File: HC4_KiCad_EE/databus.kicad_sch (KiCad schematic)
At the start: 11 parts, among them IC10 74HC4002, IC8 74HC257, IC9 74HC244, J3 Expantion_Connector

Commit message: 一部を整地
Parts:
- removed IC10: 74HC4002, Package_DIP:DIP-14_W7.62mm_Socket, symbol 74xx_2:74HC4002
- removed IC8: 74HC257, Package_DIP:DIP-16_W7.62mm_Socket, symbol 74xx_2:74HC257
- removed J3: Expantion_Connector, Connector_PinHeader_2.54mm:PinHeader_2x20_P2.54mm_Vertical, symbol Connector_Generic:Conn_02x20_Odd_Even
- removed LD4, LD5, LD6, LD7: LED, LED_THT:LED_Rectangular_W5.0mm_H2.0mm, symbol Device2:LED_
- removed RN2: 1k, Resistor_THT:R_Array_SIP5, symbol Device:R_Network04_Split
- added IC1, IC5: 74HC374, symbol 74xx_2:74HC374
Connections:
- net ALU0: now also IC9.17 (2A0)
- net ALU1: now also IC9.15 (2A1)
- net ALU2: now also IC9.13 (2A2)
- net ALU3: now also IC9.11 (2A3)
- net Databus0: now also IC9.3 (2Y0); no longer IC9.17 (2A0)
- net Databus1: now also IC9.5 (2Y1); no longer IC9.15 (2A1)
- net Databus2: now also IC9.7 (2Y2); no longer IC9.13 (2A2)
- net Databus3: now also IC9.9 (2Y3); no longer IC9.11 (2A3)
- net GND: no longer IC9.19 (2OE)
- net ~{ALU_OE}: now also IC9.19 (2OE)
- no-connect marks 22 -> 0
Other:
- note removed: "Instruction_Decoder"

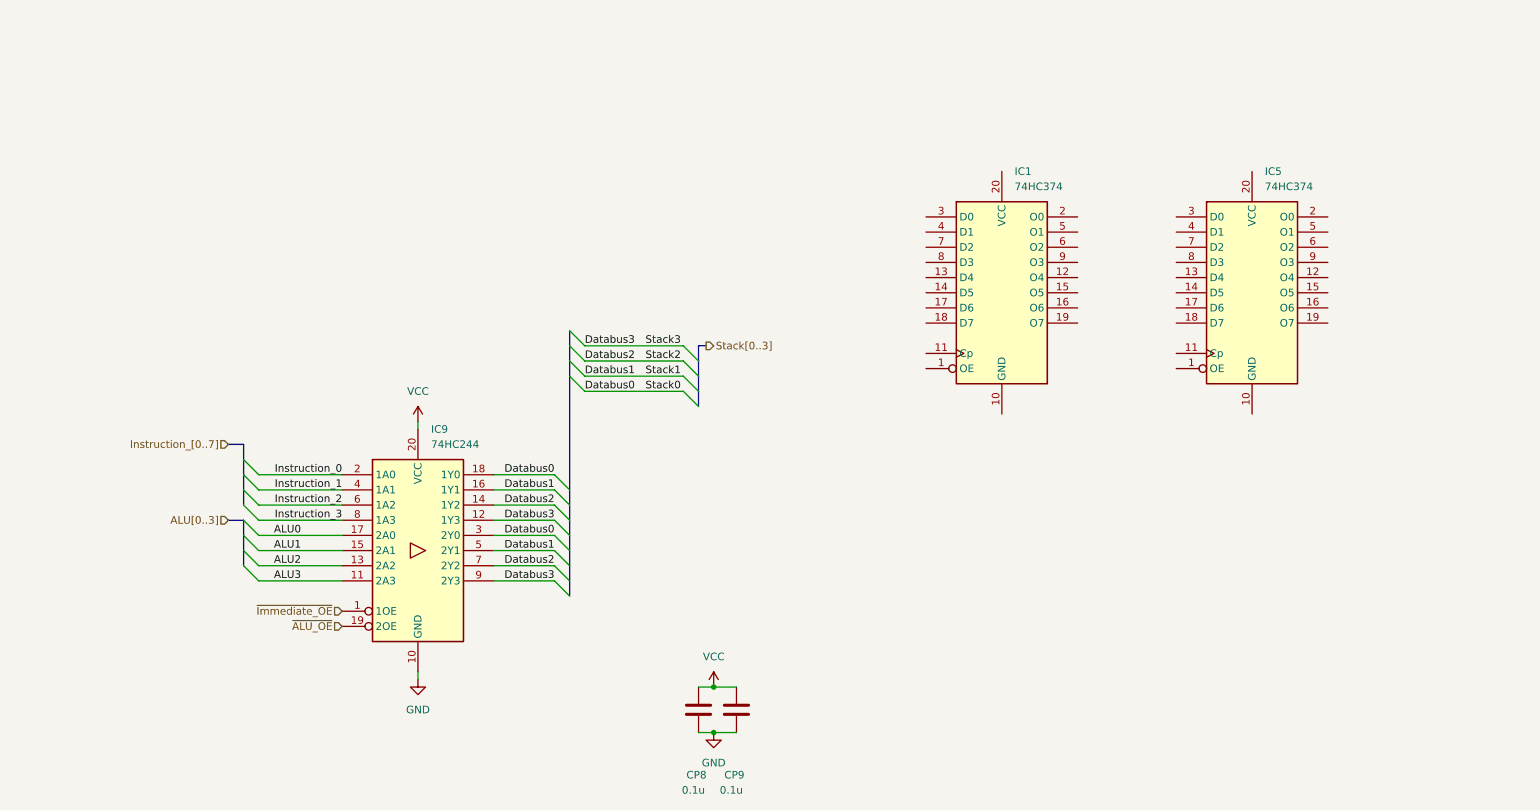
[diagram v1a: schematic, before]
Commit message: 4809を別シートに、ほか
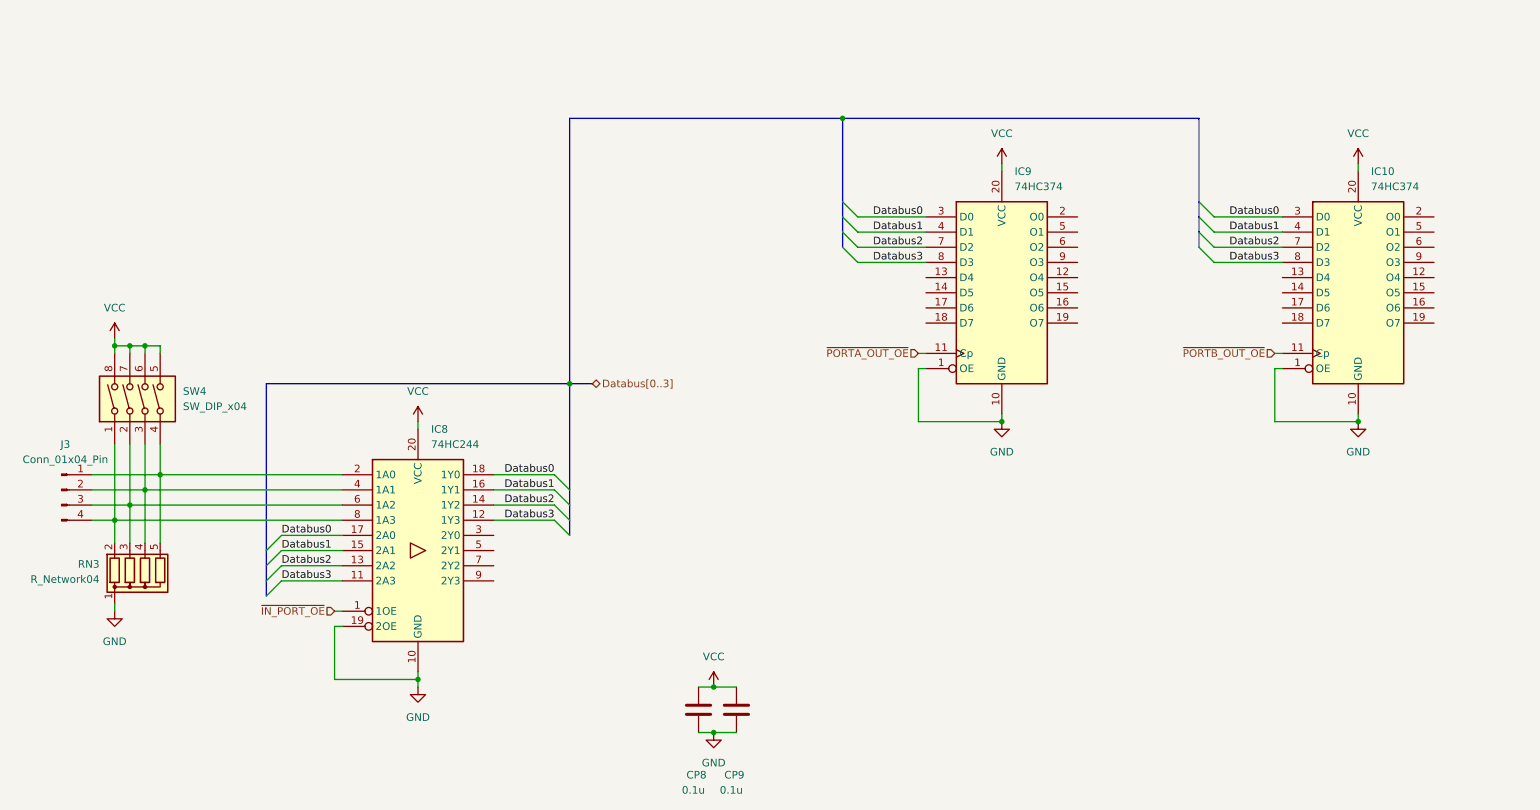
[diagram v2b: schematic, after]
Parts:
- added J3: Conn_01x04_Pin, symbol Connector:Conn_01x04_Pin
- added RN3: R_Network04, Resistor_THT:R_Array_SIP5, symbol Device:R_Network04
- added SW4: SW_DIP_x04, symbol Switch:SW_DIP_x04
- renumbered IC5 to IC10, IC9 to IC8, IC1 to IC9
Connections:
- net ALU0 is gone; now on net Databus0: IC8.17 (2A0)
- net ALU1 is gone; now on net Databus1: IC8.15 (2A1)
- net ALU2 is gone; now on net Databus2: IC8.13 (2A2)
- net ALU3 is gone; now on net Databus3: IC8.11 (2A3)
- net ~{ALU_OE} is gone; now on net GND: IC8.19 (2OE)
- net Databus0: now also IC10.3 (D0), IC9.3 (D0); no longer IC8.3 (2Y0)
- net Databus1: now also IC10.4 (D1), IC9.4 (D1); no longer IC8.5 (2Y1)
- net Databus2: now also IC10.7 (D2), IC9.7 (D2); no longer IC8.7 (2Y2)
- net Databus3: now also IC10.8 (D3), IC9.8 (D3); no longer IC8.9 (2Y3)
- net GND: now also IC10.1 (OE), IC10.10 (GND), IC9.1 (OE), IC9.10 (GND), RN3.1 (common)
- net VCC: now also IC10.20 (VCC), IC9.20 (VCC), SW4.5, SW4.6, SW4.7, SW4.8
- net ~{PORTA_OUT_OE}: now reaches IC9.11 (Cp)
- net ~{PORTB_OUT_OE}: now reaches IC10.11 (Cp)
- net Instruction_0: no longer names the net of IC8.2 (1A0)
- net Instruction_0: now also J3.1 (Pin_1), RN3.5 (R4), SW4.4
- net Instruction_1: no longer names the net of IC8.4 (1A1)
- net Instruction_1: now also J3.2 (Pin_2), RN3.4 (R3), SW4.3
- net Instruction_2: no longer names the net of IC8.6 (1A2)
- net Instruction_2: now also J3.3 (Pin_3), RN3.3 (R2), SW4.2
- net Instruction_3: no longer names the net of IC8.8 (1A3)
- net Instruction_3: now also J3.4 (Pin_4), RN3.2 (R1), SW4.1
- net ~{Immediate_OE} renamed ~{IN_PORT_OE}
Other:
- moved on the sheet: IC10

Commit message: 完成かも～
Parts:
- removed IC10, IC9: 74HC374, symbol 74xx_2:74HC374
- added CP11: 0.1u, Capacitor_THT:C_Disc_D3.0mm_W1.6mm_P2.50mm, symbol Device2:C_Bypass
- added IC6, IC7: 74HC377, symbol 74xx_2:74HC377
- added J3: Port_A, symbol Connector:Conn_01x04_Pin
- added J4: Port_B, symbol Connector:Conn_01x04_Pin
- added LD10, LD11, LD12, LD13, LD14, LD3, LD4, LD5, LD6, LD7, LD8, LD9: LED, LED_THT:LED_Rectangular_W5.0mm_H2.0mm, symbol Device2:LED_
- added RN2, RN3, RN4: 1k, Resistor_THT:R_Array_SIP9, symbol Device:R_Network08_Split
- J2: renamed from J3; value Conn_01x04_Pin -> Port_IN
- RN1: renamed from RN3; value R_Network04 -> 10k
- renumbered IC8 to IC5, SW4 to SW1
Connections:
- net Databus0: now also IC6.13 (D4), IC6.3 (D0), IC7.13 (D4), IC7.3 (D0)
- net Databus1: now also IC6.14 (D5), IC6.4 (D1), IC7.14 (D5), IC7.4 (D1)
- net Databus2: now also IC6.17 (D6), IC6.7 (D2), IC7.17 (D6), IC7.7 (D2)
- net Databus3: now also IC6.18 (D7), IC6.8 (D3), IC7.18 (D7), IC7.8 (D3)
- net GND: now also CP11.2, IC6.1 (~{E}), IC6.10 (GND), IC7.1 (~{E}), IC7.10 (GND), RN2.1 (R1), RN2.1 (R1), RN2.1 (R1), RN2.1 (R1), RN3.1 (R1), RN3.1 (R1), RN3.1 (R1), RN3.1 (R1), RN4.1 (R1), RN4.1 (R1), RN4.1 (R1), RN4.1 (R1)
- net VCC: now also CP11.1, IC6.20 (VCC), IC7.20 (VCC)
- net ~{PORTA_OUT_OE}: now also IC6.11 (CP)
- net ~{PORTB_OUT_OE}: now also IC7.11 (CP)
- net at IC5.3 (2Y0): now also LD6.2
- net at IC5.5 (2Y1): now also LD5.2
- net at IC5.7 (2Y2): now also LD4.2
- net at IC5.9 (2Y3): now also LD3.2
- new net: LD13.1 (K), RN4.4 (R3.2)
- new net: LD5.1 (K), RN2.4 (R3.2)
- new net: LD10.1 (K), RN3.5 (R4.2)
- new net: IC6.12 (Q4), LD10.2
- new net: LD14.1 (K), RN4.5 (R4.2)
- new net: IC7.12 (Q4), LD14.2
- new net: IC7.15 (Q5), LD13.2
- new net: LD12.1 (K), RN4.3 (R2.2)
- new net: LD6.1 (K), RN2.5 (R4.2)
- new net: IC6.15 (Q5), LD9.2
- new net: IC6.16 (Q6), LD8.2
- new net: IC6.19 (Q7), LD7.2
- new net: IC6.2 (Q0), J3.1 (Pin_1)
- new net: IC6.5 (Q1), J3.2 (Pin_2)
- new net: IC6.6 (Q2), J3.3 (Pin_3)
- new net: IC6.9 (Q3), J3.4 (Pin_4)
- new net: IC7.16 (Q6), LD12.2
- new net: IC7.2 (Q0), J4.1 (Pin_1)
- new net: IC7.5 (Q1), J4.2 (Pin_2)
- new net: IC7.6 (Q2), J4.3 (Pin_3)
- new net: IC7.9 (Q3), J4.4 (Pin_4)
- new net: LD8.1 (K), RN3.3 (R2.2)
- new net: LD11.1 (K), RN4.2 (R1.2)
- new net: LD9.1 (K), RN3.4 (R3.2)
- new net: IC7.19 (Q7), LD11.2
- new net: LD4.1 (K), RN2.3 (R2.2)
- new net: LD7.1 (K), RN3.2 (R1.2)
- new net: LD3.1 (K), RN2.2 (R1.2)

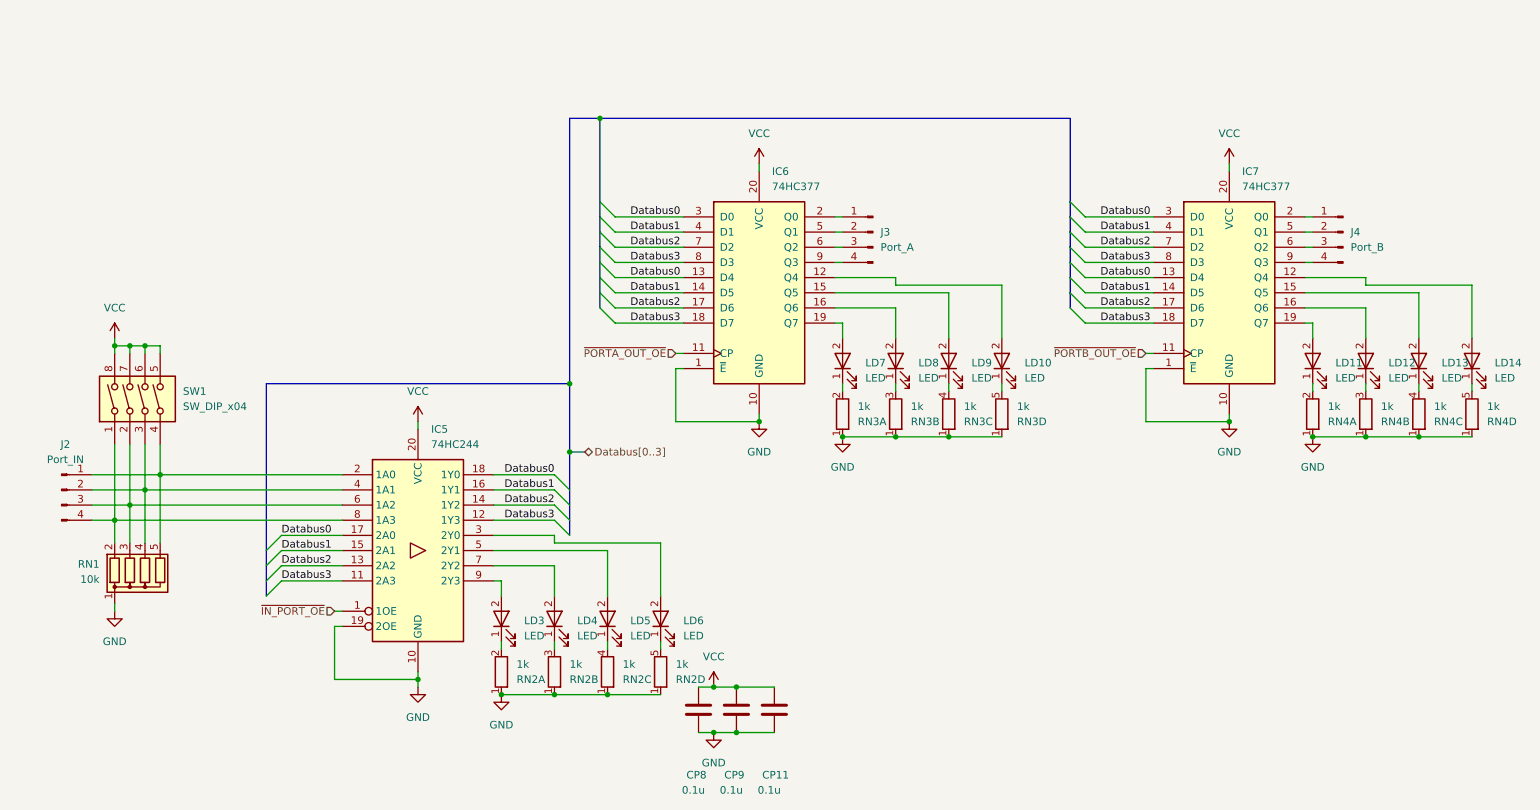
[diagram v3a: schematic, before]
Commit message: Carry_ENを論理反転、回路図の修正
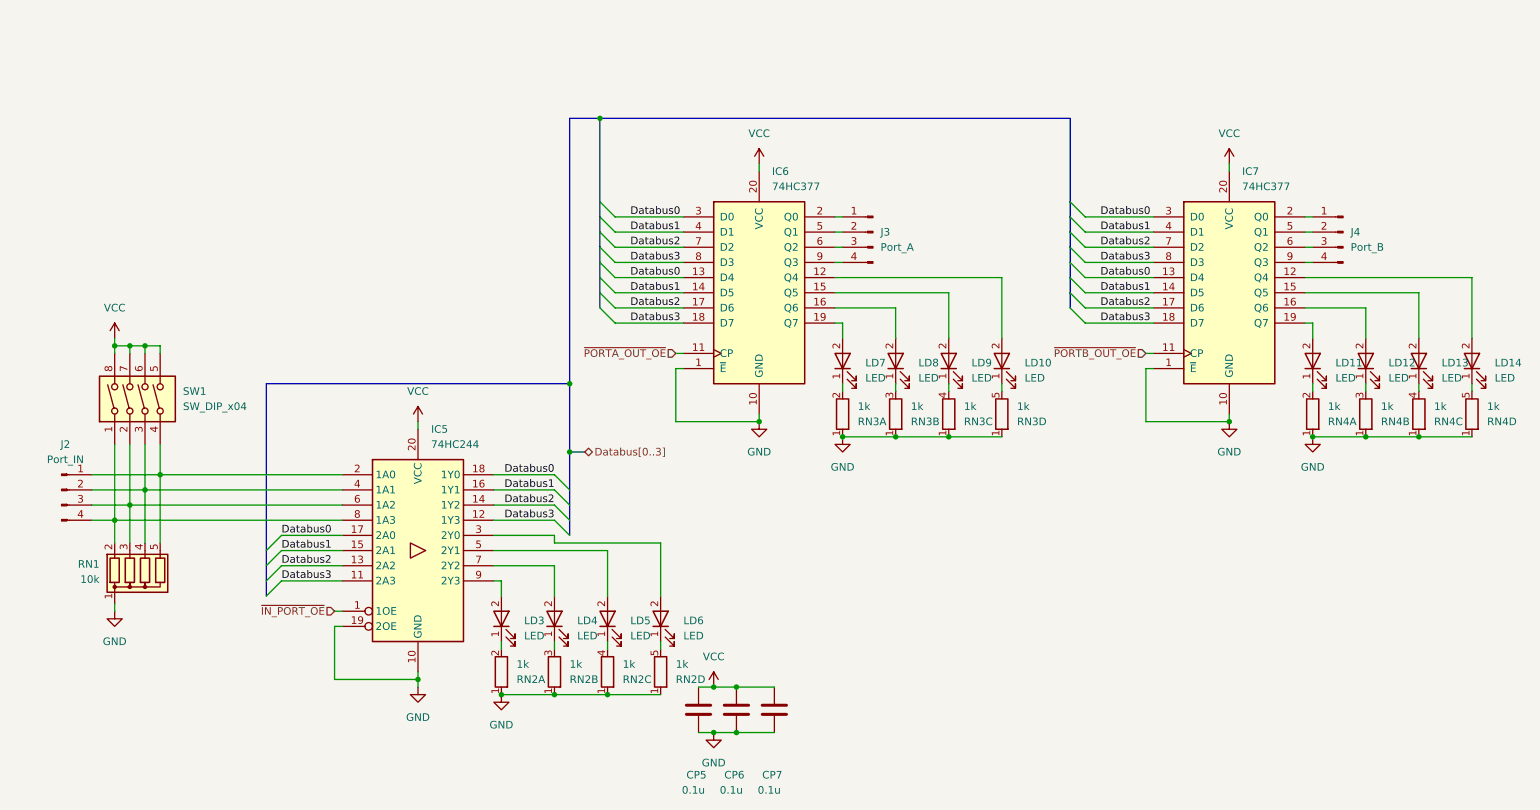
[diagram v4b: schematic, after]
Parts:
- renumbered CP8 to CP5, CP9 to CP6, CP11 to CP7
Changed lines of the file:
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@@
 	(wire
 		(pts
-			(xy 168.91 87.63) (xy 179.07 87.63)
+			(xy 168.91 87.63) (xy 196.85 87.63)
 		)
 		(stroke
@@
 	(wire
 		(pts
-			(xy 275.59 88.9) (xy 275.59 97.79)
+			(xy 275.59 87.63) (xy 275.59 97.79)
 		)
 		(stroke
@@
 	(wire
 		(pts
-			(xy 257.81 87.63) (xy 257.81 88.9)
-		)
-		(stroke
-			(width 0)
-			(type default)
-		)
-	)
-	(wire
-		(pts
 			(xy 132.08 95.25) (xy 143.51 95.25)
 		)
@@
 	(wire
 		(pts
-			(xy 257.81 88.9) (xy 275.59 88.9)
-		)
-		(stroke
-			(width 0)
-			(type default)
-		)
-	)
-	(wire
-		(pts
 			(xy 210.82 80.01) (xy 222.25 80.01)
 		)
@@
 	(wire
 		(pts
-			(xy 196.85 88.9) (xy 196.85 97.79)
+			(xy 196.85 87.63) (xy 196.85 97.79)
 		)
 		(stroke
@@
 		)
 	)
-	(wire
-		(pts
-			(xy 179.07 87.63) (xy 179.07 88.9)
-		)
-		(stroke
-			(width 0)
-			(type default)
-		)
-	)
-	(wire
-		(pts
-			(xy 179.07 88.9) (xy 196.85 88.9)
-		)
-		(stroke
-			(width 0)
-			(type default)
-		)
-	)
 	(bus
 		(pts
@@
 	(wire
 		(pts
-			(xy 247.65 87.63) (xy 257.81 87.63)
+			(xy 247.65 87.63) (xy 275.59 87.63)
 		)
 		(stroke
@@
 		(on_board yes)
 		(dnp no)
-		(property "Reference" "CP8"
+		(property "Reference" "CP5"
 			(at 144.018 170.942 0)
 			(effects
@@
 			(project "HC4_KiCad"
 				(path "/33731ded-38c0-4297-bdd8-92b082f46ff8/294cbb59-ed60-4be2-81ec-3da02c446083"
-					(reference "CP8")
+					(reference "CP5")
 					(unit 1)
 				)
@@
 		(on_board yes)
 		(dnp no)
-		(property "Reference" "CP11"
+		(property "Reference" "CP7"
 			(at 156.718 170.942 0)
 			(effects
@@
 			(project "HC4_KiCad_EE"
 				(path "/33731ded-38c0-4297-bdd8-92b082f46ff8/294cbb59-ed60-4be2-81ec-3da02c446083"
-					(reference "CP11")
+					(reference "CP7")
 					(unit 1)
 				)
@@
 		(on_board yes)
 		(dnp no)
-		(property "Reference" "CP9"
+		(property "Reference" "CP6"
 			(at 150.368 170.942 0)
 			(effects
@@
 			(project "HC4_KiCad"
 				(path "/33731ded-38c0-4297-bdd8-92b082f46ff8/294cbb59-ed60-4be2-81ec-3da02c446083"
-					(reference "CP9")
+					(reference "CP6")
 					(unit 1)
 				)

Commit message: PortBを4511に、フットプリントの割り付け開始
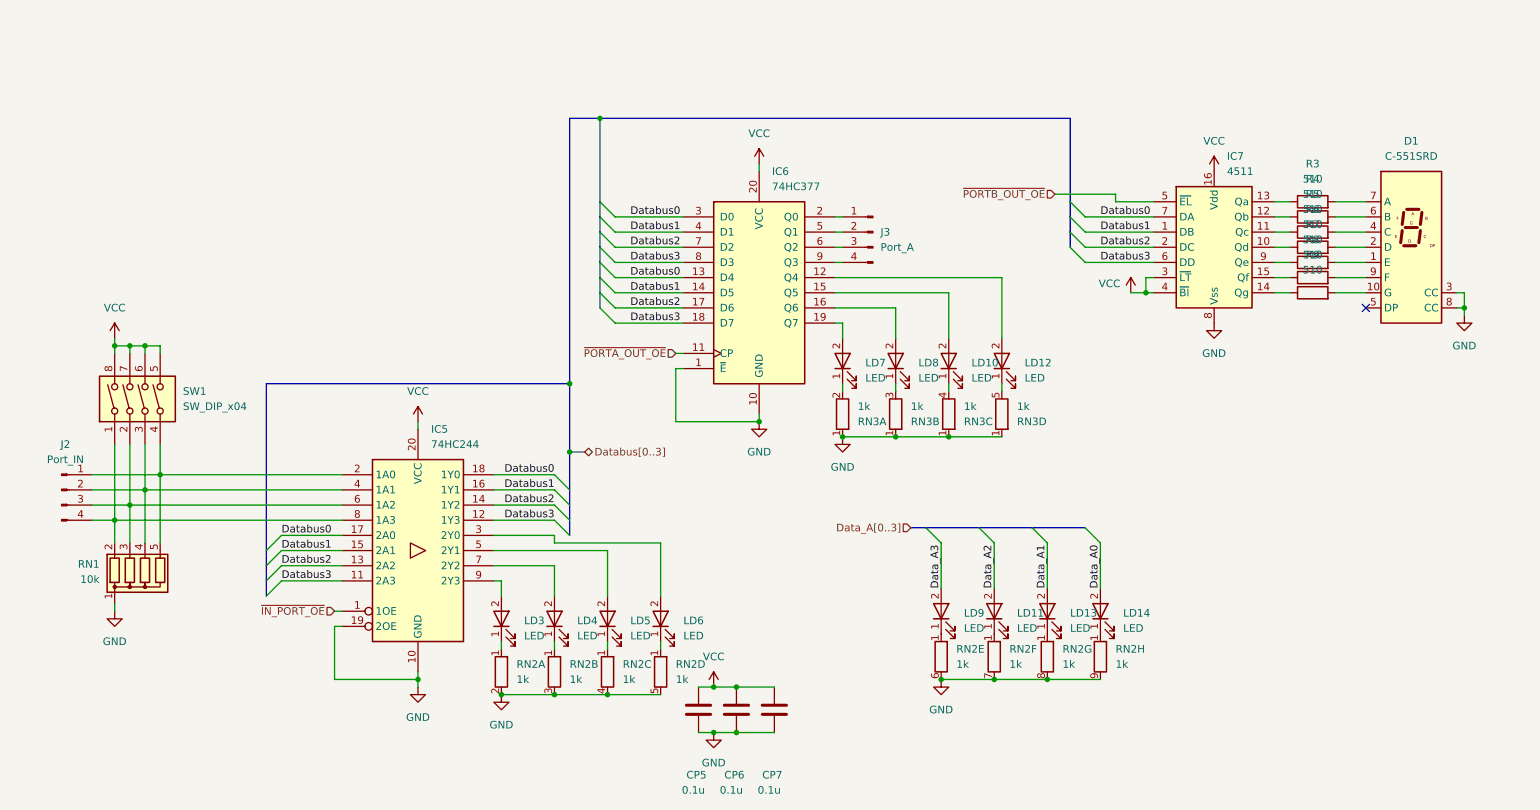
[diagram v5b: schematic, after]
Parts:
- removed IC7: 74HC377, symbol 74xx_2:74HC377
- removed J4: Port_B, symbol Connector:Conn_01x04_Pin
- removed LD12: LED, LED_THT:LED_Rectangular_W5.0mm_H2.0mm, symbol Device2:LED_
- removed RN4: 1k, Resistor_THT:R_Array_SIP9, symbol Device:R_Network08_Split
- added D1: C-551SRD, Display_7Segment:D1X8K, symbol Display_Character:D168K
- added IC7: 4511, symbol 4xxx_IEEE:4511
- added LD9: LED, LED_THT:LED_Rectangular_W5.0mm_H2.0mm, symbol Device2:LED_
- added R3, R4, R5, R6, R7, R8, R9: 510, symbol Device:R
- added unit 6 of RN2
- added unit 8 of RN2
- added unit 7 of RN2
- added unit 5 of RN2
- CP5, CP6, CP7: footprint Capacitor_THT:C_Disc_D3.0mm_W1.6mm_P2.50mm -> Capacitor_SMD:C_0603_1608Metric
- IC5: footprint Package_DIP:DIP-20_W7.62mm_Socket -> Package_SO:SOP-20_7.5x12.8mm_P1.27mm
- IC6: footprint (none) -> Package_SO:SOP-20_7.5x12.8mm_P1.27mm
- renumbered LD9 to LD10, LD10 to LD12
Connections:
- net Databus0: now also IC7.7 (DA)
- net Databus1: now also IC7.1 (DB)
- net Databus2: now also IC7.2 (DC)
- net Databus3: now also IC7.6 (DD)
- net GND: now also RN2.2 (R1.2), RN2.3 (R2.2), RN2.4 (R3.2), RN2.5 (R4.2), D1.3 (CC), D1.8 (CC), IC7.8 (Vss), RN2.6 (R5.2), RN2.7 (R6.2), RN2.8 (R7.2), RN2.9 (R8.2); no longer RN2.1 (R1), RN2.1 (R1), RN2.1 (R1), RN2.1 (R1)
- net VCC: now also IC7.16 (Vdd), IC7.3 (~{LT}), IC7.4 (~{BI})
- net ~{PORTB_OUT_OE}: now also IC7.5 (~{EL})
- net at LD13.1 (K): now also RN2.1 (R1)
- net at LD5.1 (K): now also RN2.1 (R1); no longer RN2.4 (R3.2)
- net at LD14.1 (K): now also RN2.1 (R1)
- net Data_A0: now reaches LD14.2
- net Data_A1: now reaches LD13.2
- net at LD6.1 (K): now also RN2.1 (R1); no longer RN2.5 (R4.2)
- net at LD11.1 (K): now also RN2.1 (R1)
- net Data_A2: now reaches LD11.2
- net at LD4.1 (K): now also RN2.1 (R1); no longer RN2.3 (R2.2)
- net at LD3.1 (K): now also RN2.1 (R1); no longer RN2.2 (R1.2)
- new net: IC7.14 (Qg), R9.1
- new net: D1.10 (G), R9.2
- new net: D1.1 (E), R7.2
- new net: D1.2 (D), R6.2
- new net: D1.4 (C), R5.2
- new net: D1.6 (B), R4.2
- new net: D1.7 (A), R3.2
- new net: D1.9 (F), R8.2
- new net: IC7.15 (Qf), R8.1
- new net: IC7.11 (Qc), R5.1
- new net: IC7.10 (Qd), R6.1
- new net: IC7.12 (Qb), R4.1
- new net: IC7.13 (Qa), R3.1
- new net: IC7.9 (Qe), R7.1
- new net: LD9.1 (K), RN2.1 (R1)
- new net Data_A3: LD9.2
- no-connect marks 0 -> 1
